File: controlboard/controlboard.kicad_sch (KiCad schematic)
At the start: 7 parts, among them J1 Conn_02x08_Odd_Even, J2 Conn_02x08_Odd_Even, U1 74HC163, U2 74HCT245, U3 74HCT245

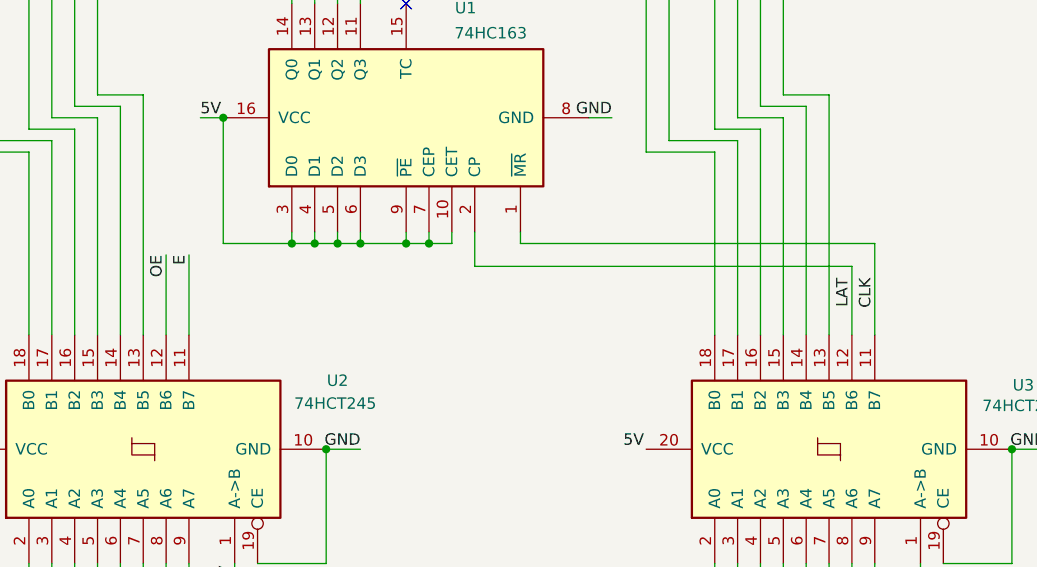
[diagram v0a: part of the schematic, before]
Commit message: Modify control board to allow latching without progressing line
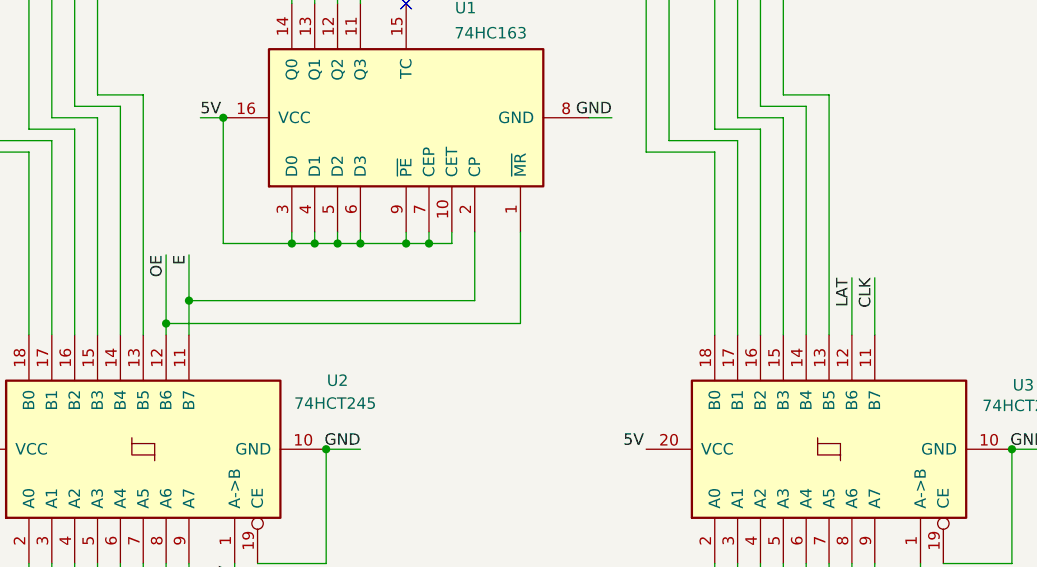
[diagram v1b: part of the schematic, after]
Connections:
- net CLK: no longer U1.1 (~{MR})
- net E: now also U1.2 (CP)
- net LAT: no longer U1.2 (CP)
- net OE: now also U1.1 (~{MR})
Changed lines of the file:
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@@
+	)
+	(junction
+		(at 59.69 90.17)
+		(diameter 0)
+		(color 0 0 0 0)
 	)
 	(junction
@@
 		(color 0 0 0 0)
 	)
+	(junction
+		(at 62.23 87.63)
+		(diameter 0)
+		(color 0 0 0 0)
+	)
 	(no_connect
 		(at 86.36 54.61)
@@
 	(wire
 		(pts
+			(xy 59.69 90.17) (xy 99.06 90.17)
+		)
+		(stroke
+			(width 0)
+			(type default)
+		)
+	)
+	(wire
+		(pts
 			(xy 88.9 161.29) (xy 88.9 166.37)
 		)
@@
 	(wire
 		(pts
-			(xy 59.69 82.55) (xy 59.69 91.44)
+			(xy 59.69 82.55) (xy 59.69 90.17)
 		)
 		(stroke
@@
 	(wire
 		(pts
-			(xy 93.98 80.01) (xy 93.98 83.82)
-		)
-		(stroke
-			(width 0)
-			(type default)
-		)
-	)
-	(wire
-		(pts
 			(xy 111.76 161.29) (xy 111.76 166.37)
 		)
@@
 	(wire
 		(pts
+			(xy 59.69 90.17) (xy 59.69 91.44)
+		)
+		(stroke
+			(width 0)
+			(type default)
+		)
+	)
+	(wire
+		(pts
 			(xy 91.44 80.01) (xy 91.44 81.28)
 		)
@@
 	(wire
 		(pts
+			(xy 93.98 80.01) (xy 93.98 87.63)
+		)
+		(stroke
+			(width 0)
+			(type default)
+		)
+	)
+	(wire
+		(pts
 			(xy 120.65 41.91) (xy 120.65 68.58)
 		)
@@
 	(wire
 		(pts
+			(xy 138.43 85.09) (xy 138.43 91.44)
+		)
+		(stroke
+			(width 0)
+			(type default)
+		)
+	)
+	(wire
+		(pts
 			(xy 73.66 161.29) (xy 73.66 166.37)
 		)
@@
 	(wire
 		(pts
-			(xy 99.06 80.01) (xy 99.06 81.28)
-		)
-		(stroke
-			(width 0)
-			(type default)
-		)
-	)
-	(wire
-		(pts
-			(xy 62.23 82.55) (xy 62.23 91.44)
+			(xy 99.06 80.01) (xy 99.06 90.17)
+		)
+		(stroke
+			(width 0)
+			(type default)
+		)
+	)
+	(wire
+		(pts
+			(xy 62.23 82.55) (xy 62.23 87.63)
 		)
 		(stroke
@@
 	(wire
 		(pts
-			(xy 138.43 81.28) (xy 138.43 91.44)
+			(xy 62.23 87.63) (xy 62.23 91.44)
 		)
 		(stroke
@@
 	(wire
 		(pts
+			(xy 135.89 85.09) (xy 135.89 91.44)
+		)
+		(stroke
+			(width 0)
+			(type default)
+		)
+	)
+	(wire
+		(pts
 			(xy 133.35 64.77) (xy 133.35 91.44)
 		)
@@
 	(wire
 		(pts
-			(xy 135.89 83.82) (xy 135.89 91.44)
-		)
-		(stroke
-			(width 0)
-			(type default)
-		)
-	)
-	(wire
-		(pts
 			(xy 63.5 67.31) (xy 66.04 67.31)
 		)
@@
 	(wire
 		(pts
-			(xy 93.98 83.82) (xy 135.89 83.82)
-		)
-		(stroke
-			(width 0)
-			(type default)
-		)
-	)
-	(wire
-		(pts
 			(xy 49.53 116.84) (xy 49.53 128.27)
 		)
@@
 	(wire
 		(pts
+			(xy 62.23 87.63) (xy 93.98 87.63)
+		)
+		(stroke
+			(width 0)
+			(type default)
+		)
+	)
+	(wire
+		(pts
 			(xy 52.07 67.31) (xy 46.99 67.31)
 		)
@@
 		)
 		(stroke
-			(width 0)
-			(type default)
-		)
-	)
-	(wire
-		(pts
-			(xy 99.06 81.28) (xy 138.43 81.28)
-		)
-		(stroke

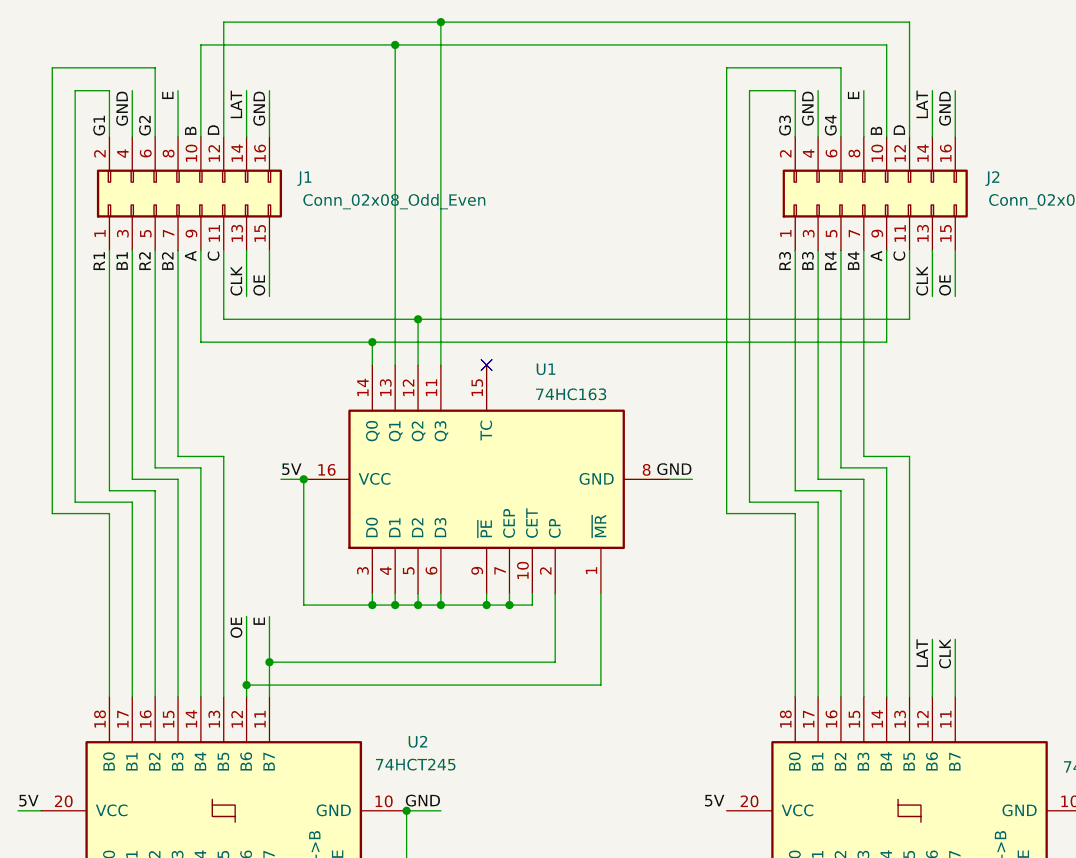
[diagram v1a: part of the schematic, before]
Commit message: Rewire GPIO for ease of programming
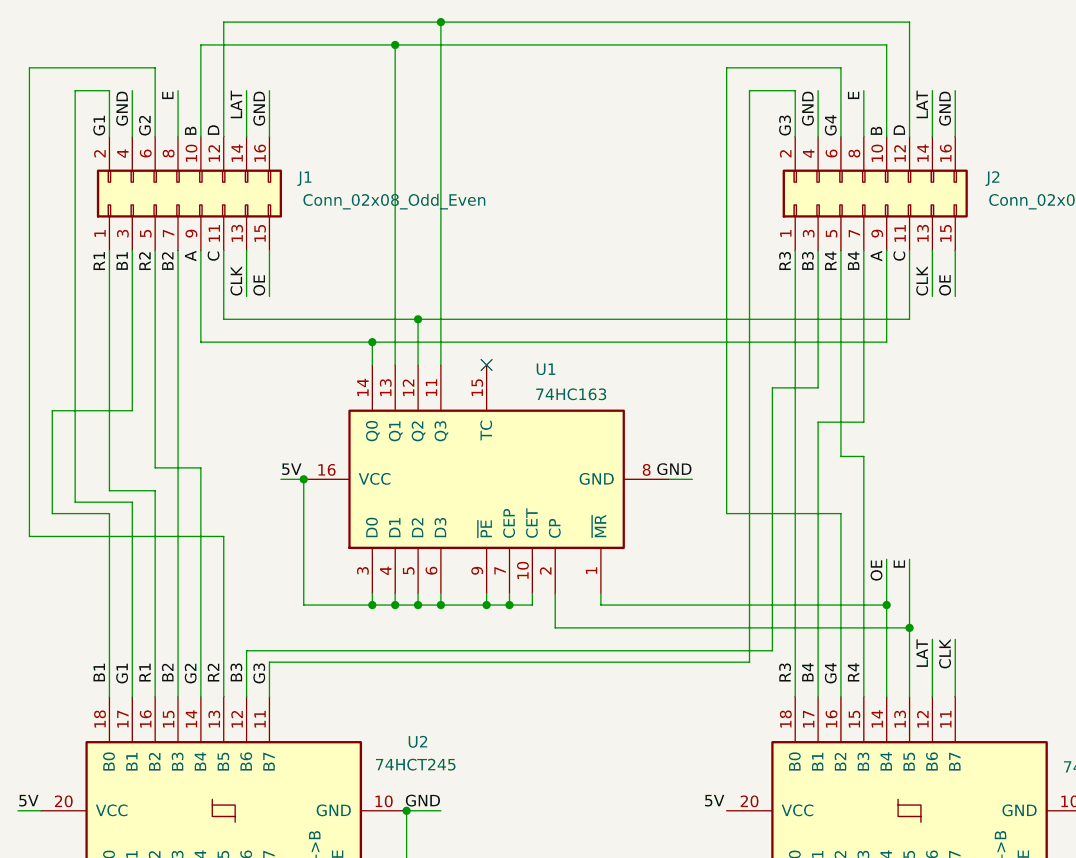
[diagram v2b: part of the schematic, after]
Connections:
- net R2 is gone; now on net G2: J1.5 (Pin_5), U2.14 (B4)
- net B1: now also U2.18 (B0); no longer U2.15 (B3)
- net B2: now also U2.15 (B3); no longer U2.13 (B5)
- net B3: now also U2.12 (B6); no longer U3.15 (B3)
- net B4: now also U3.17 (B1); no longer U3.13 (B5)
- net E: now also U3.13 (B5); no longer U2.11 (B7)
- net G2: now also U2.13 (B5); no longer U2.18 (B0)
- net G3: now also U2.11 (B7); no longer U3.17 (B1)
- net G4: now also U3.16 (B2); no longer U3.18 (B0)
- net OE: now also U3.14 (B4); no longer U2.12 (B6)
- net R3: now also U3.18 (B0); no longer U3.16 (B2)
- net R4: now also U3.15 (B3); no longer U3.14 (B4)

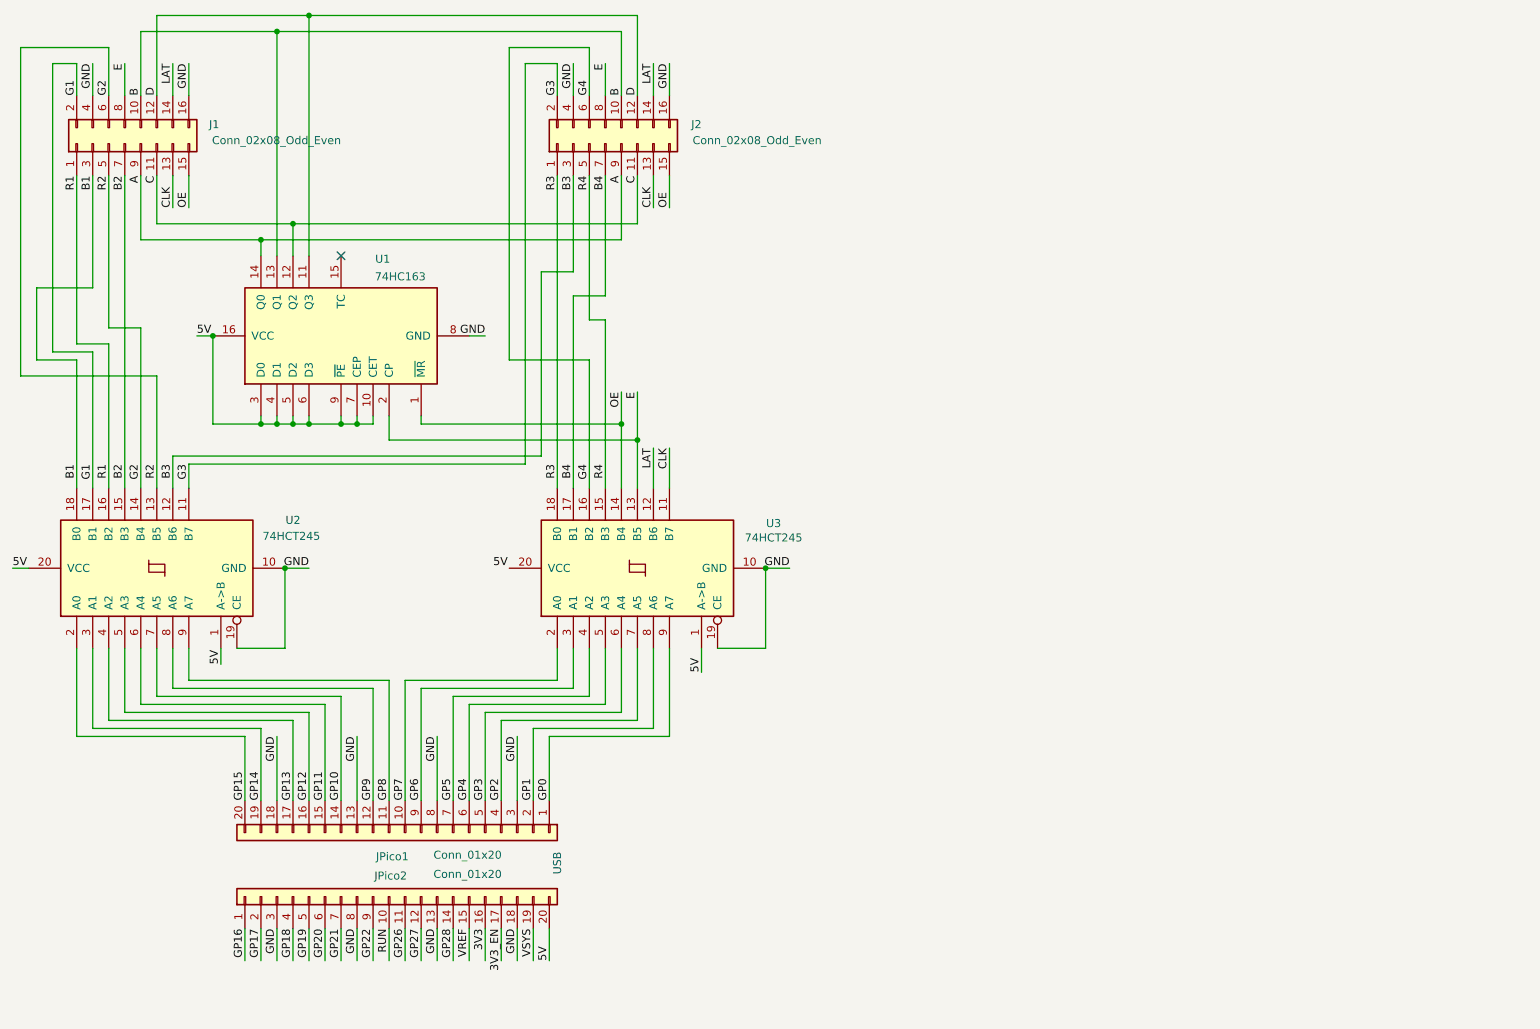
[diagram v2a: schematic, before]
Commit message: Pico receives pixel data from FPGA
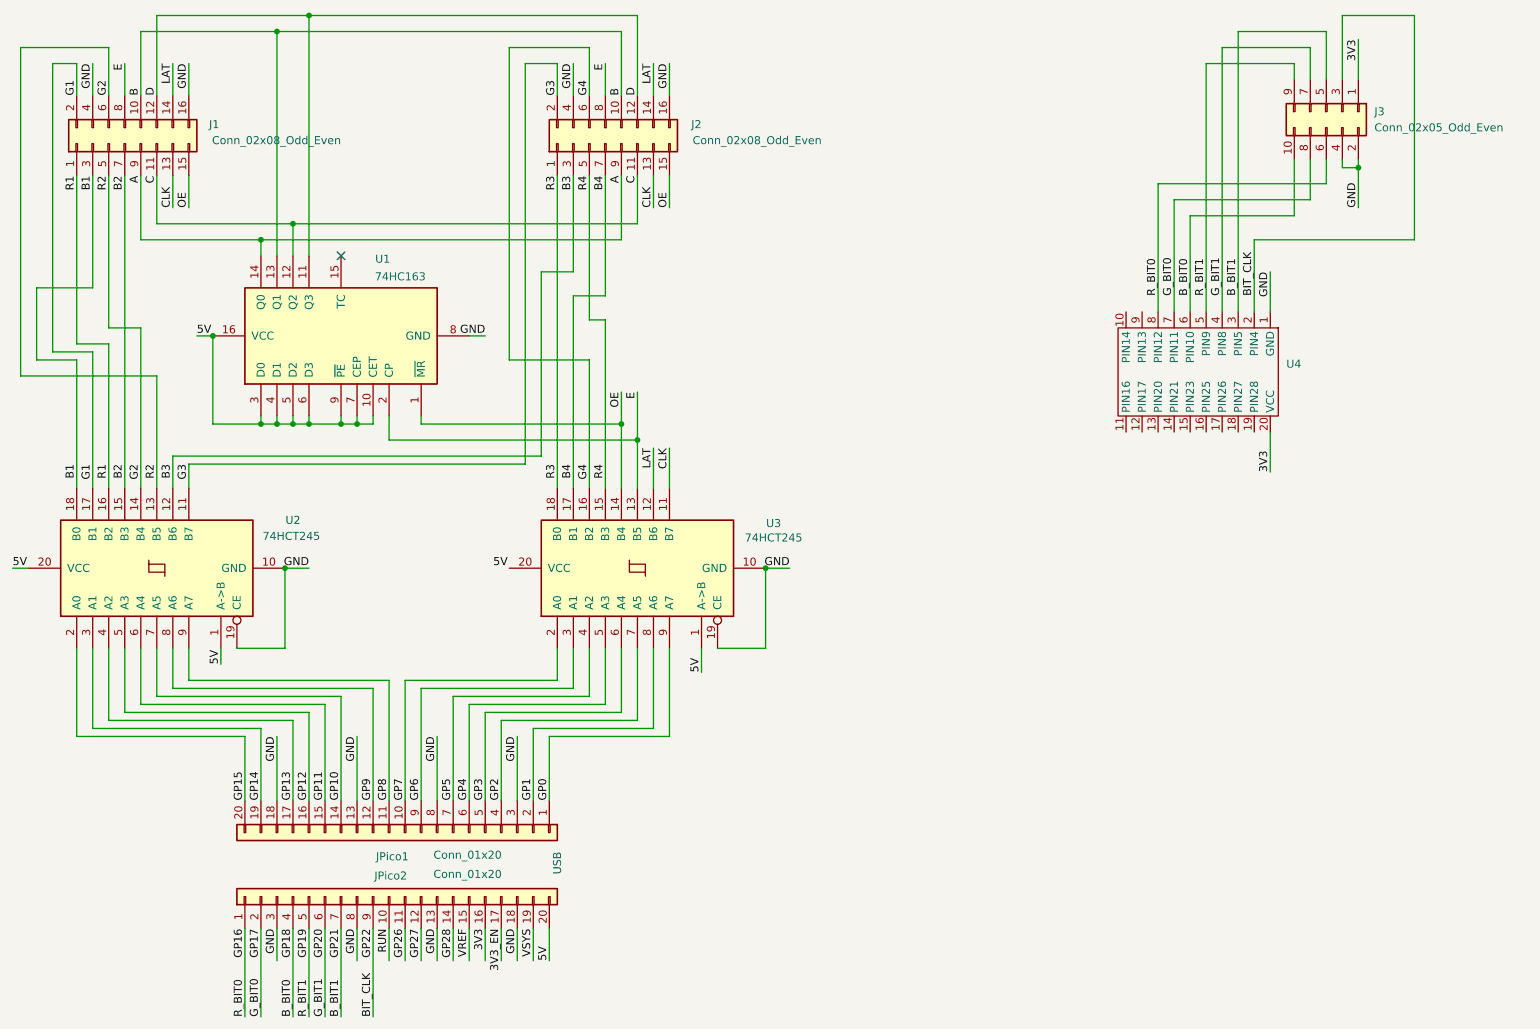
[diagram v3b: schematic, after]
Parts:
- added J3: Conn_02x05_Odd_Even, symbol Connector_Generic:Conn_02x05_Odd_Even
- added U4: ~, symbol New_Library:FPGA_DIP20
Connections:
- net 3V3: now also J3.1 (Pin_1), U4.20 (VCC)
- net GND: now also J3.2 (Pin_2), J3.4 (Pin_4), U4.1 (GND)
- net GP16: now also J3.6 (Pin_6), U4.8 (PIN12)
- net GP17: now also J3.8 (Pin_8), U4.7 (PIN11)
- net GP19: now also J3.9 (Pin_9), U4.5 (PIN9)
- net GP20: now also J3.7 (Pin_7), U4.4 (PIN8)
- net GP18 renamed B_BIT0
- net B_BIT0: now also J3.10 (Pin_10), U4.6 (PIN10)
- net GP21 renamed B_BIT1
- net B_BIT1: now also J3.5 (Pin_5), U4.3 (PIN5)
- net GP22 renamed BIT_CLK
- net BIT_CLK: now also J3.3 (Pin_3), U4.2 (PIN4)

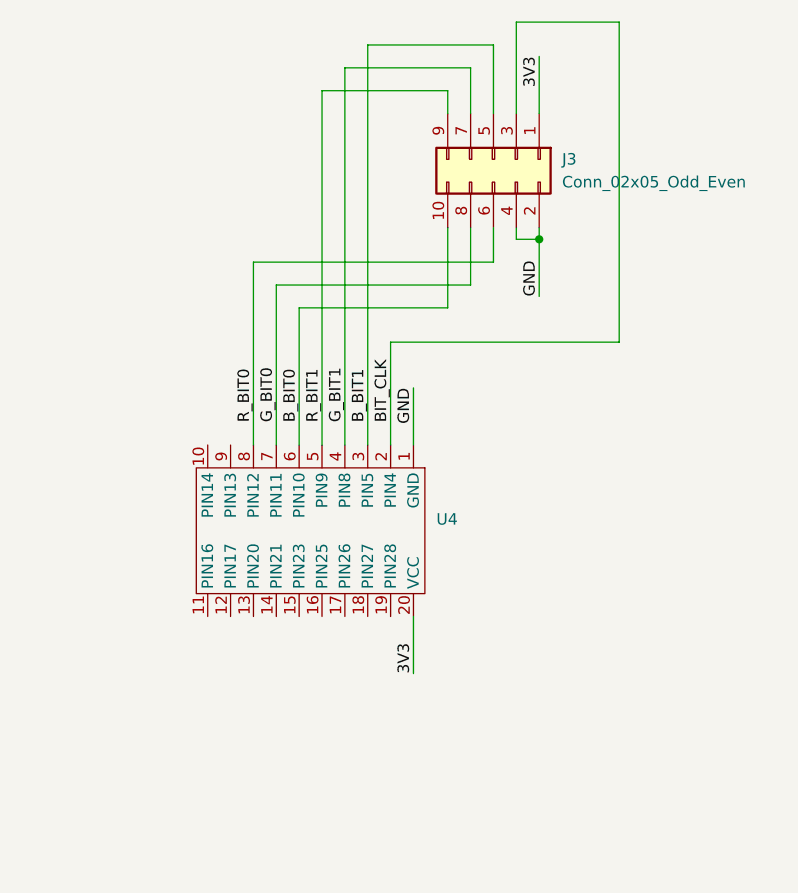
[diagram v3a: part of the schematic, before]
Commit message: Change assignment for connector cable
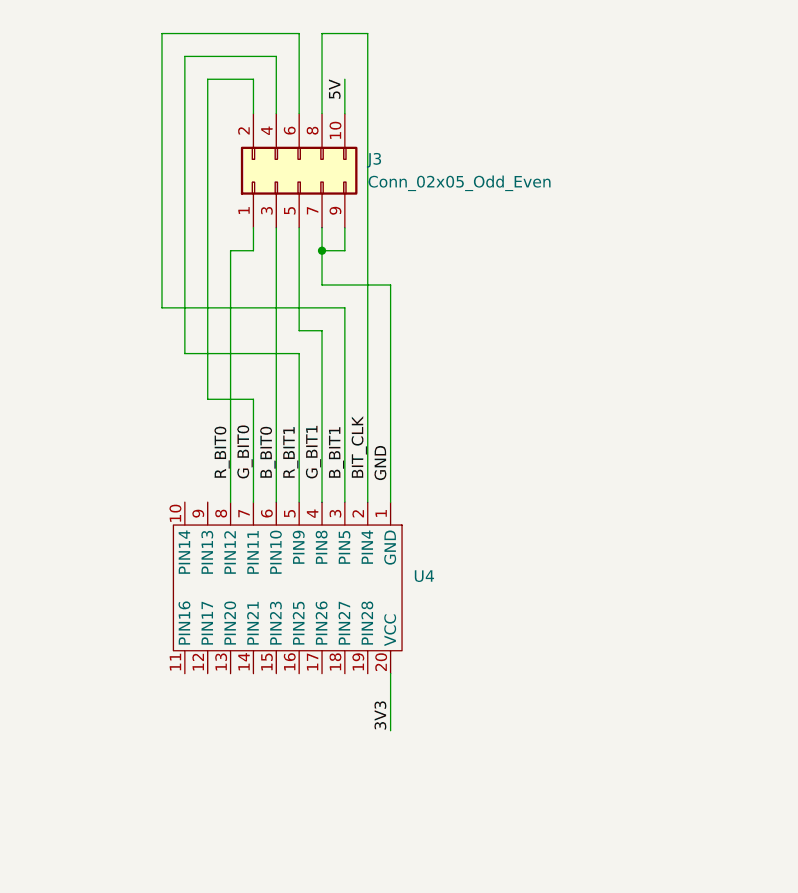
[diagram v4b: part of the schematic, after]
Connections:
- net 3V3: no longer J3.1 (Pin_1)
- net 5V: now also J3.10 (Pin_10)
- net BIT_CLK: now also J3.8 (Pin_8); no longer J3.3 (Pin_3)
- net B_BIT0: now also J3.3 (Pin_3); no longer J3.10 (Pin_10)
- net B_BIT1: now also J3.6 (Pin_6); no longer J3.5 (Pin_5)
- net GND: now also J3.7 (Pin_7), J3.9 (Pin_9); no longer J3.2 (Pin_2), J3.4 (Pin_4)
- net GP16: now also J3.1 (Pin_1); no longer J3.6 (Pin_6)
- net GP17: now also J3.2 (Pin_2); no longer J3.8 (Pin_8)
- net GP19: now also J3.4 (Pin_4); no longer J3.9 (Pin_9)
- net GP20: now also J3.5 (Pin_5); no longer J3.7 (Pin_7)
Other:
- moved on the sheet: J3, U4
